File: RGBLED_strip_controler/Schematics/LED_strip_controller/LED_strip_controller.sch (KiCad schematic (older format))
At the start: 4 parts

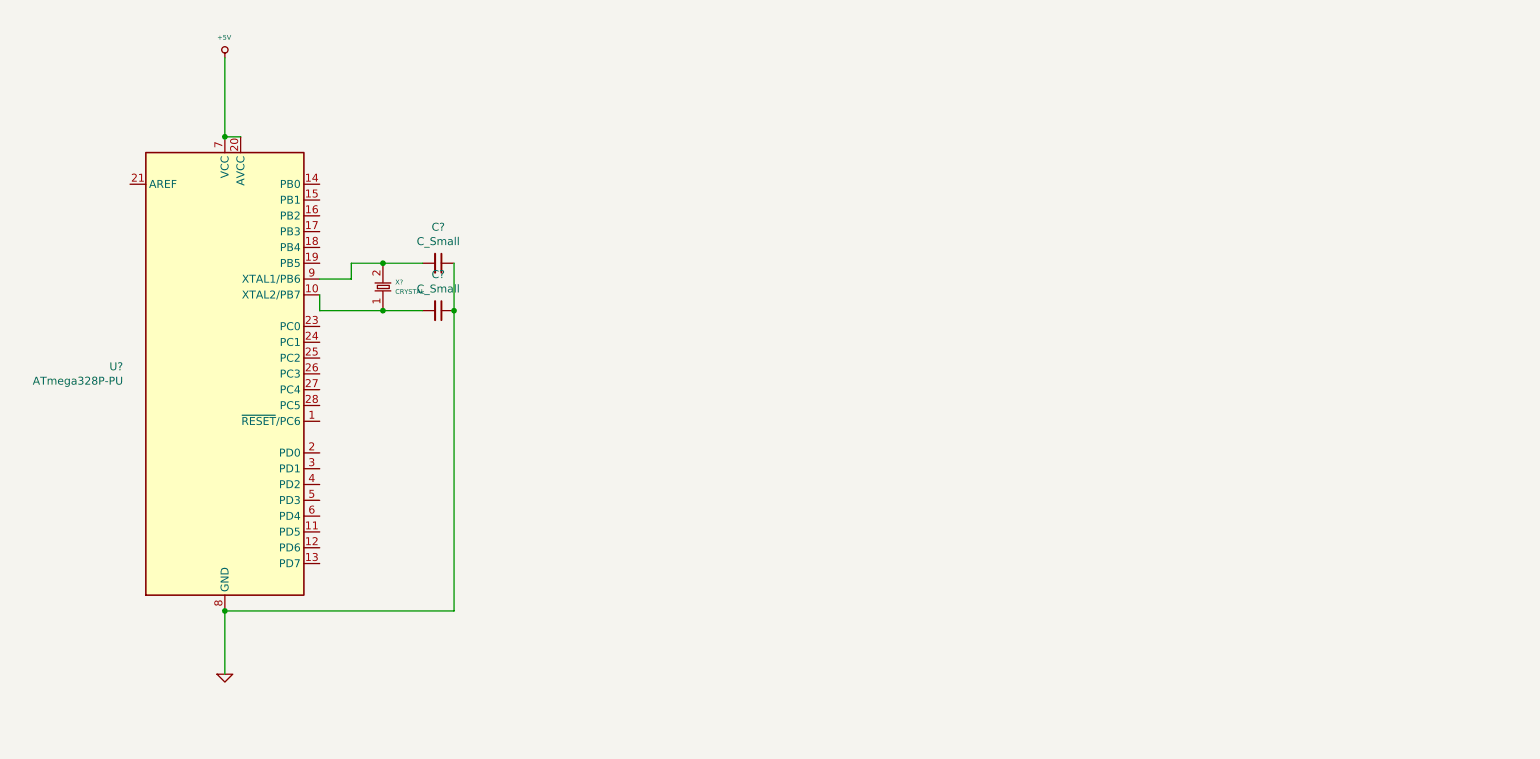
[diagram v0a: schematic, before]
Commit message: Update to schematic
Schematic updated(incomplete)
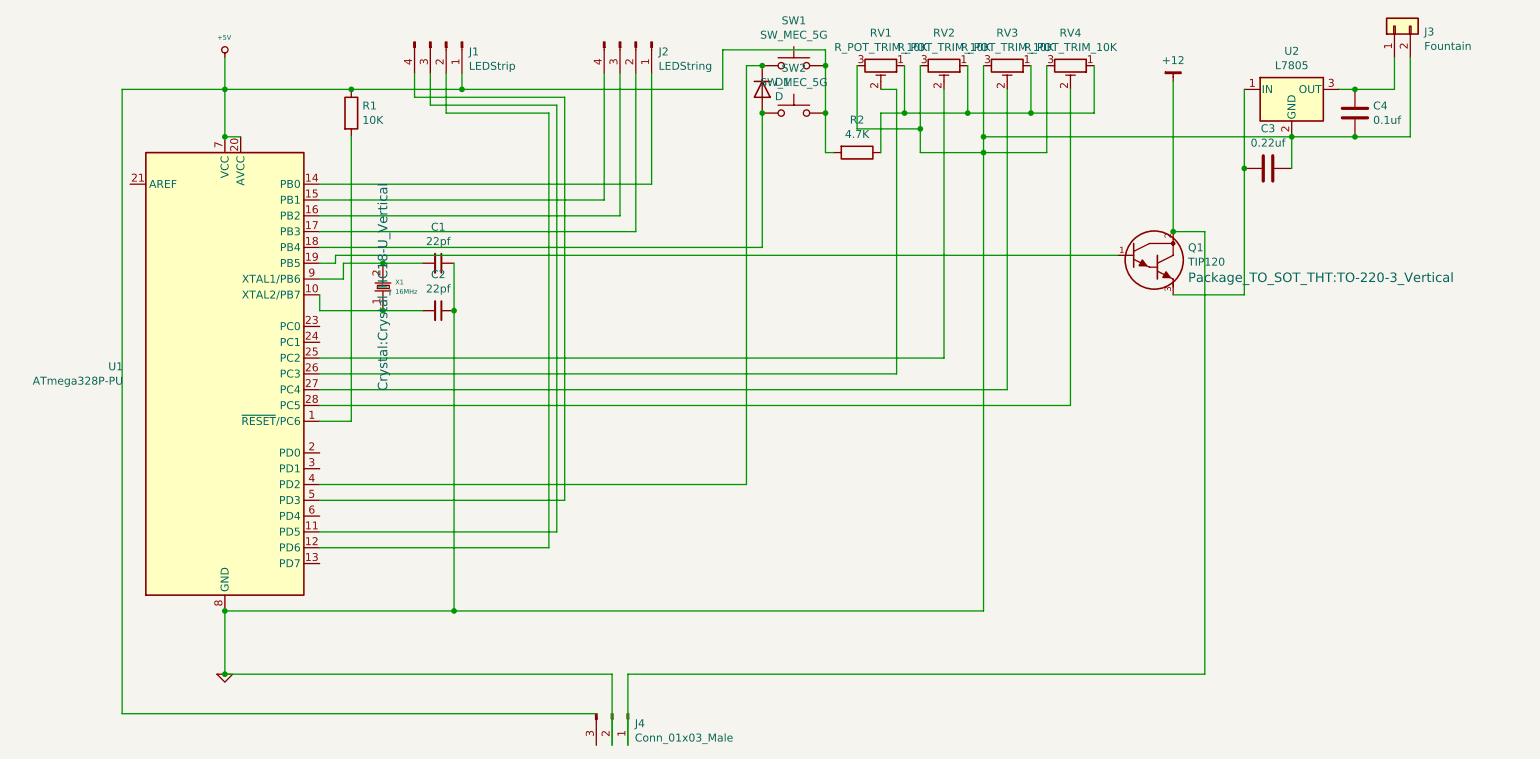
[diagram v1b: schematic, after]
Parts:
- added C3: 0.22uf, Capacitor_THT:CP_Radial_D4.0mm_P2.00mm, symbol Device:C
- added C4: 0.1uf, Capacitor_THT:CP_Radial_D4.0mm_P2.00mm, symbol Device:C
- added D1: D, Diode_THT:D_DO-34_SOD68_P2.54mm_Vertical_AnodeUp, symbol Device:D
- added J1: LEDStrip, Connector_PinHeader_1.00mm:PinHeader_1x04_P1.00mm_Vertical, symbol Connector:Conn_01x04_Male
- added J2: LEDString, Connector_PinHeader_1.00mm:PinHeader_1x04_P1.00mm_Vertical, symbol Connector:Conn_01x04_Male
- added J3: Fountain, Connector_PinHeader_1.27mm:PinHeader_1x02_P1.27mm_Vertical, symbol Connector_Generic:Conn_01x02
- added J4: Conn_01x03_Male, Connector_PinHeader_1.27mm:PinHeader_1x03_P1.27mm_Vertical, symbol Connector:Conn_01x03_Male
- added Q1: TIP120, Package_TO_SOT_THT:TO-220-3_Vertical, symbol semi-trans-generic:TIP120
- added R1: 10K, Resistor_THT:R_Axial_DIN0204_L3.6mm_D1.6mm_P2.54mm_Vertical, symbol Device:R
- added R2: 4.7K, Resistor_THT:R_Axial_DIN0204_L3.6mm_D1.6mm_P2.54mm_Vertical, symbol Device:R
- added RV1, RV2, RV3, RV4: R_POT_TRIM_10K, Potentiometer_THT:Potentiometer_Bourns_3296W_Vertical, symbol Device:R_POT_TRIM
- added SW1, SW2: SW_MEC_5G, Button_Switch_THT:SW_MEC_5GTH9, symbol Switch:SW_MEC_5G
- added U2: L7805, Package_TO_SOT_THT:TO-220-3_Vertical, symbol Regulator_Linear:L7805
- C1, C2: renamed from C?; value C_Small -> 22pf; footprint (none) -> Capacitor_THT:C_Disc_D3.0mm_W1.6mm_P2.50mm
- X1: renamed from X?; value CRYSTAL -> 16MHz; footprint (none) -> Crystal:Crystal_HC18-U_Vertical
- gave numbers to parts that had none: 1
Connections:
- net +5V: now also J1.1 (Pin_1), R1.1, R2.2, SW1.3 (B), SW1.4 (B), SW2.3 (B), SW2.4 (B)
- net GND: now also C3.1, C4.2, J3.2 (Pin_2), J4.2 (Pin_2), RV1.3, RV2.3, RV3.3, RV4.3, U2.2 (GND)
- net at U1.1 (~RESET~/PC6): now also R1.2
- net at U1.11 (PD5): now also U1.12 (PD6), J1.2 (Pin_2), J1.3 (Pin_3)
- net at U1.14 (PB0): now also J2.1 (Pin_1)
- net at U1.15 (PB1): now also J2.4 (Pin_4)
- net at U1.16 (PB2): now also J2.3 (Pin_3)
- net at U1.17 (PB3): now also J2.2 (Pin_2)
- net at U1.18 (PB4): now also D1.2 (A), SW2.1 (A), SW2.2 (A)
- net at U1.19 (PB5): now also Q1.1 (B)
- net at U1.25 (PC2): now also RV2.2
- net at U1.26 (PC3): now also RV1.2
- net at U1.27 (PC4): now also RV3.2
- net at U1.28 (PC5): now also RV4.2
- net at U1.4 (PD2): now also D1.1 (K), SW1.1 (A), SW1.2 (A)
- net at U1.5 (PD3): now also J1.4 (Pin_4)
- new net: R2.1, RV1.1, RV2.1, RV3.1, RV4.1
- new net: C3.2, Q1.3 (E), U2.1 (IN)
- new net: C4.1, J3.1 (Pin_1), U2.3 (OUT)
- new net +12: J4.1 (Pin_1), Q1.2 (C)

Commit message: Schematic update
Corrected an error I made.
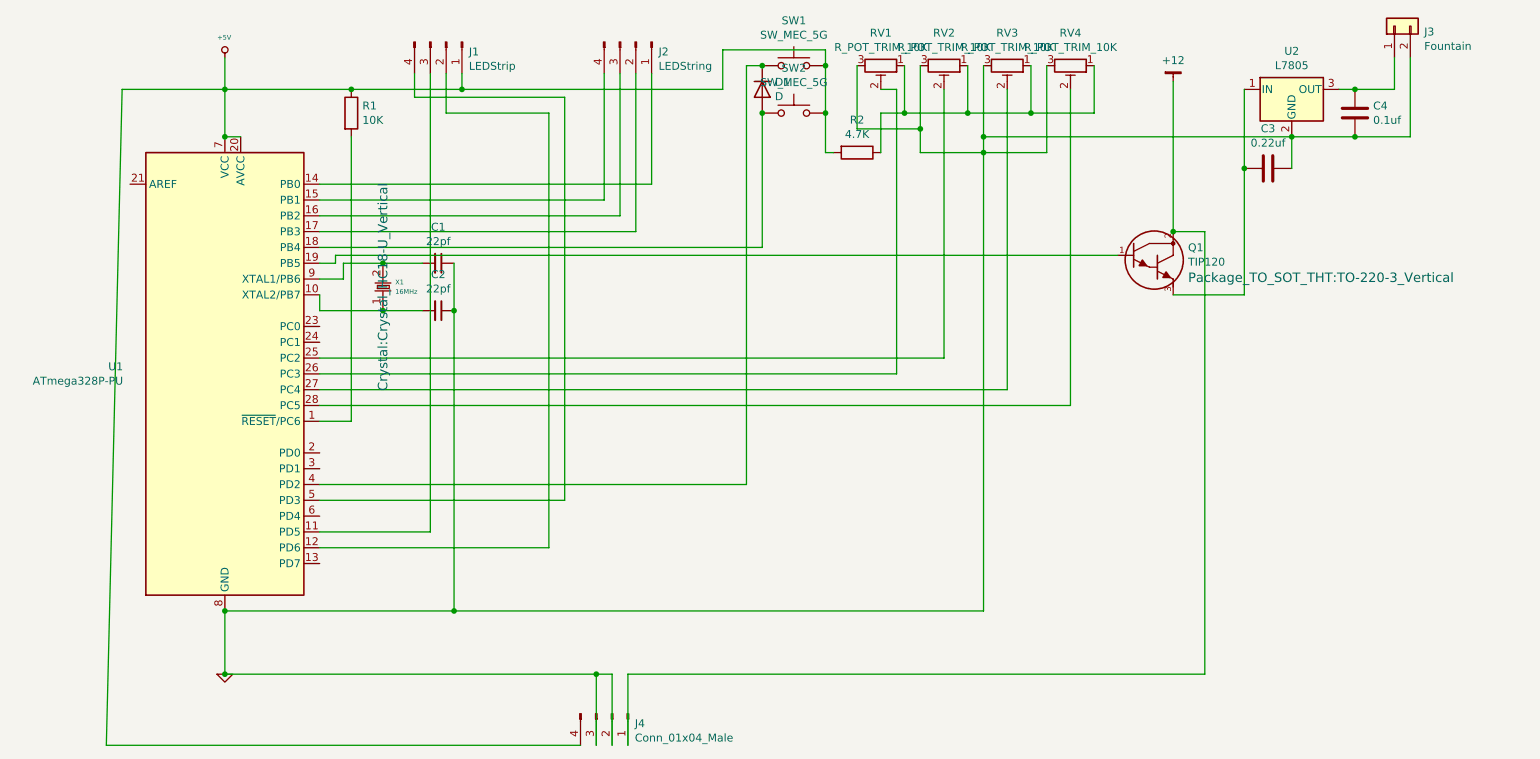
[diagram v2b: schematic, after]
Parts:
- removed J4: Conn_01x03_Male, Connector_PinHeader_1.27mm:PinHeader_1x03_P1.27mm_Vertical, symbol Connector:Conn_01x03_Male
- added J4: Conn_01x04_Male, symbol Connector:Conn_01x04_Male
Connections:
- net +12: now also J4.1 (Pin_1)
- net +5V: now also J4.4 (Pin_4)
- net GND: now also J4.2 (Pin_2), J4.3 (Pin_3)
- net at J1.3 (Pin_3), U1.11 (PD5): no longer J1.2 (Pin_2), U1.12 (PD6)
- new net: J1.2 (Pin_2), U1.12 (PD6)
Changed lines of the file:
@@
 Wire Wire Line
 	2100 4000 3550 4000
-Wire Wire Line
-	2800 1200 2800 1000
-Wire Wire Line
-	3600 1200 2800 1200
-Wire Wire Line
-	3600 3900 3600 1200
-Wire Wire Line
-	3550 1250 3550 3900
-Wire Wire Line
-	3550 3900 3600 3900
-Wire Wire Line
-	3550 4000 3550 3900
-Wire Wire Line
-	2100 3900 3550 3900
 $Comp
 L Connector:Conn_01x04_Male J2
@@
 	4650 850  5300 850
 Wire Wire Line
-	5300 850  5300 950
-Connection ~ 5300 950
-Wire Wire Line
-	5300 950  5300 1250
-Wire Wire Line
 	2100 2100 4900 2100
 Wire Wire Line
@@
 $EndComp
 Wire Wire Line
-	5300 1250 5300 1500
-Wire Wire Line
 	5300 1500 5350 1500
-Connection ~ 5300 1250
 Wire Wire Line
 	5650 1250 5800 1250
@@
 Wire Wire Line
 	8250 1600 8250 1400
-$Comp
-L Connector:Conn_01x03_Male J4
-U 1 1 5F1CE618
+Wire Wire Line
+	7500 2000 7700 2000
+Wire Wire Line
+	7700 2000 7700 4800
+Wire Wire Line
+	7700 4800 4050 4800
+Wire Wire Line
+	4050 4800 4050 5250
+Connection ~ 7500 2000
+Wire Wire Line
+	3950 5250 3950 4800
+Wire Wire Line
+	3950 4800 3850 4800
+Connection ~ 1500 4800
+Wire Wire Line
+	3750 5250 750  5250
+Wire Wire Line
+	750  5250 850  1100
+Wire Wire Line
+	850  1100 1500 1100
+Wire Wire Line
+	3550 1250 3550 4000
+Wire Wire Line
+	2100 3900 2800 3900
+Wire Wire Line
+	2800 3900 2800 1000
+Wire Wire Line
+	5300 1250 5300 1500
+Connection ~ 5300 1250
+Wire Wire Line
+	5300 950  5300 1250
+Wire Wire Line
+	5300 850  5300 950
+Connection ~ 5300 950
+$Comp
+L Connector:Conn_01x04_Male J4
+U 1 1 5F18E76E
 P 3950 5050
 F 0 "J4" V 4012 5194 50  0000 L CNN
-F 1 "Conn_01x03_Male" V 4103 5194 50  0000 L CNN
-F 2 "Connector_PinHeader_1.27mm:PinHeader_1x03_P1.27mm_Vertical" H 3950 5050 50  0001 C CNN
+F 1 "Conn_01x04_Male" V 4103 5194 50  0000 L CNN
+F 2 "" H 3950 5050 50  0001 C CNN
 F 3 "~" H 3950 5050 50  0001 C CNN
 	1    3950 5050
@@
 $EndComp
 Wire Wire Line
-	7500 2000 7700 2000
-Wire Wire Line
-	7700 2000 7700 4800
-Wire Wire Line
-	7700 4800 4050 4800
-Wire Wire Line
-	4050 4800 4050 5250
-Connection ~ 7500 2000
-Wire Wire Line
-	3950 5250 3950 4800
-Wire Wire Line
-	3950 4800 1500 4800
-Connection ~ 1500 4800
-Wire Wire Line
-	3850 5050 850  5050
-Wire Wire Line
-	850  5050 850  1100
-Wire Wire Line
-	850  1100 1500 1100
+	3850 4800 3850 5250
+Connection ~ 3850 4800
+Wire Wire Line
+	3850 4800 1500 4800
 $EndSCHEMATC
